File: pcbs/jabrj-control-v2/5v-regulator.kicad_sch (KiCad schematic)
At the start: 46 parts, among them Q401 DMN21D2UFB-7B, Q402 DMN21D2UFB-7B, Q403 DMN21D2UFB-7B, U401 AZV3001FZ4-7, U402 TPS259472ARPWR, U403 MAX20008AFOC/VY+T

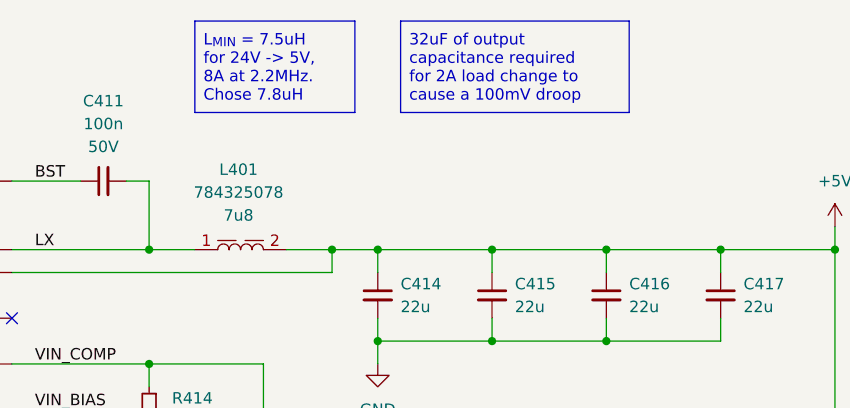
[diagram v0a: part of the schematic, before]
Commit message: Fixed 5V buck inductor value
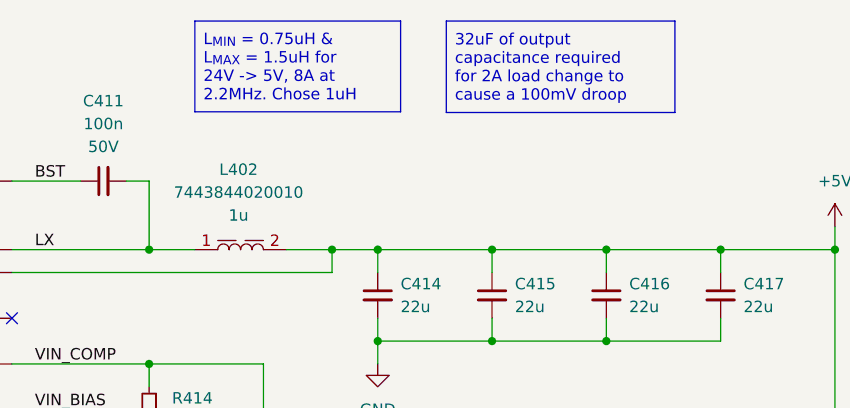
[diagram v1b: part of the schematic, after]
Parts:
- removed L401: 784325078, project_footprints:784325078, symbol PWR-IND:784325078
- added L402: 7443844020010, project_footprints:L_Wurth_WE-MXGI-4020, symbol PWR-IND:4020_7443844020010
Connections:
- net +5V: now also L402.2
- net LX: now also L402.1

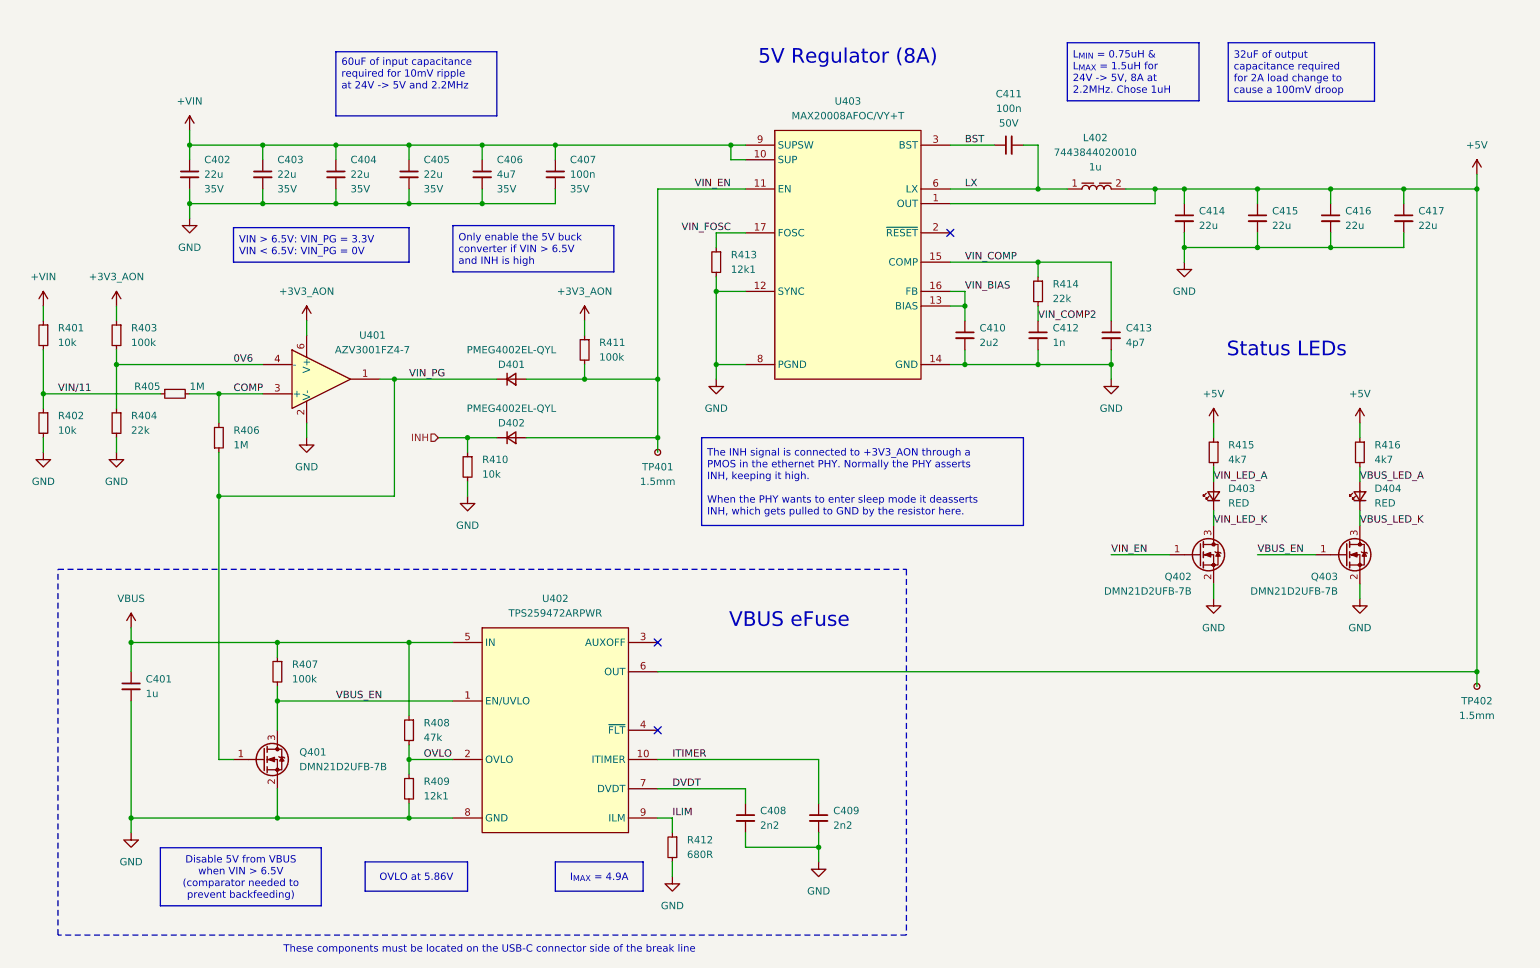
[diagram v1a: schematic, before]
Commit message: Minor schematic fixes
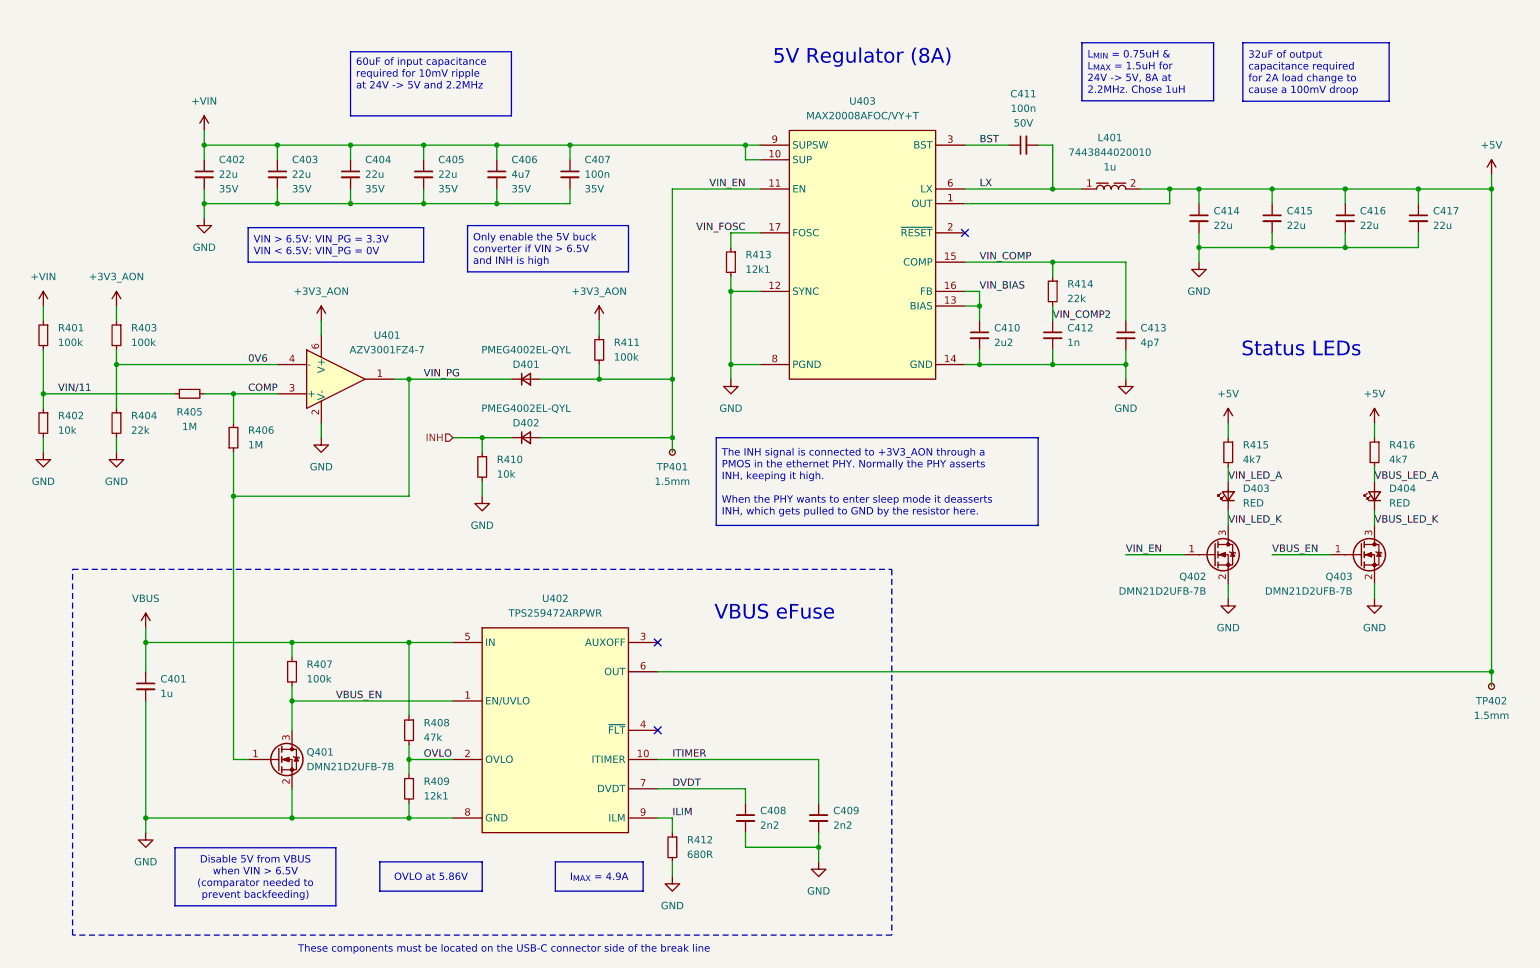
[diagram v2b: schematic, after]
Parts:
- R401: value 10k -> 100k
- renumbered L402 to L401
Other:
- moved on the sheet: C401, C402, C403, C404, C405, C406, C407, C410, C411, C412, C413, C414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

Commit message: Layout started
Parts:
- C406: footprint project_footprints:C_0805 -> project_footprints:C_0603
- C407: footprint project_footprints:C_0402 -> project_footprints:C_0603; Voltage 35V -> 100V
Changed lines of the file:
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@@
 			)
 		)
-		(property "Footprint" "project_footprints:C_0805"
+		(property "Footprint" "project_footprints:C_0603"
 			(at 101.6 53.34 0)
 			(hide yes)
@@
 			)
 		)
-		(property "Footprint" "project_footprints:C_0402"
+		(property "Footprint" "project_footprints:C_0603"
 			(at 114.3 53.34 0)
 			(hide yes)
@@
 			)
 		)
-		(property "Voltage" "35V"
+		(property "Voltage" "100V"
 			(at 116.84 55.8738 0)
 			(show_name no)

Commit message: Layout almost done
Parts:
- D403, D404: footprint (none) -> project_footprints:C_0402
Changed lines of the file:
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@@
 			)
 		)
-		(property "Footprint" ""
+		(property "Footprint" "project_footprints:C_0402"
 			(at 228.6 109.22 90)
 			(hide yes)
@@
 			)
 		)
-		(property "Footprint" ""
+		(property "Footprint" "project_footprints:C_0402"
 			(at 254 109.22 90)
 			(hide yes)

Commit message: 651 Unrouted
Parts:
- D403, D404: footprint project_footprints:C_0402 -> project_footprints:LED_0402
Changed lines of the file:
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@@
 	(text_box "60uF of input capacitance required for 10mV ripple at 24V -> 5V and 2.2MHz"
 		(exclude_from_sim no)
-		(at 76.2 32.0439 0)
-		(size 27.94 11.1361)
+		(at 73.66 32.044 0)
+		(size 30.48 8.596)
 		(margins 0.9525 0.9525 0.9525 0.9525)
 		(stroke
@@
 				(size 1.27 1.27)
 			)
-			(justify left top)
+			(justify left)
 		)
 	)
@@
 			)
 		)
-		(property "Footprint" "project_footprints:C_0402"
+		(property "Footprint" "project_footprints:LED_0402"
 			(at 228.6 109.22 90)
 			(hide yes)
@@
 			)
 		)
-		(property "Footprint" "project_footprints:C_0402"
+		(property "Footprint" "project_footprints:LED_0402"
 			(at 254 109.22 90)
 			(hide yes)

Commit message: 603 Unrouted
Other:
- moved on the sheet: C402, C403, C404, C405, C406, C407, C410, C411, C412, C413, C414, C415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

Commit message: 400 Unrouted
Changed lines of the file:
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@@
-		(color 0 0 0 0)
-	)
-	(junction
-		(at 86.36 104.14)
-		(diameter 0)
 		(color 0 0 0 0)
 	)
@@
 		(pts
 			(xy 96.52 93.98) (xy 101.6 93.98)
-		)
-		(stroke
-			(width 0)
-			(type default)
-		)
-	)
-	(wire
-		(pts
-			(xy 86.36 104.14) (xy 88.9 104.14)
 		)
 		(stroke
@@
 		)
 	)
-	(hierarchical_label "VIN_PG"
-		(shape output)
-		(at 88.9 104.14 0)
-		(effects
-			(font
-				(size 1.27 1.27)
-			)
-			(justify left)
-		)
-	)

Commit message: 133 Unrouted
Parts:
- added C418: 100n, project_footprints:C_0402, symbol DEV:C_SMALL
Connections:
- net 0V6: now also C418.1
- net GND: now also C418.2
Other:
- moved on the sheet: C401, C402, C403, C404, C405, C406, C407, C408, C409, C410, C411, C412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
